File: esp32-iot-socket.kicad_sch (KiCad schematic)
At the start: 2 parts, among them J1 Conn_01x01_Pin, J2 Conn_01x01_Socket

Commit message: viper22as, transformer, hierarchical connections
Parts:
- removed J1: Conn_01x01_Pin, symbol Connector:Conn_01x01_Pin
- removed J2: Conn_01x01_Socket, symbol Connector:Conn_01x01_Socket
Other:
- sheet Microcontroller Section ports: added 3.3V in, Gnd in, TRIAC output, ZV signal in; removed none
- sheet Power Supply Section ports: added 3.3V out, Gnd out, TRIAC in, ZV signal out; removed none
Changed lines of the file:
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@@
 (kicad_sch (version 20230121) (generator eeschema)
   (paper "A4")
-  (symbol (lib_id "Connector:Conn_01x01_Socket") (at 124.46 107.95 0) (unit 1)
-    (in_bom yes) (on_board yes) (dnp no) (fields_autoplaced)
-    (property "Reference" "J2" (at 125.73 106.68 0)
+  (wire (pts (xy 120.65 91.44) (xy 156.21 91.44))
+    (stroke (width 0) (type default))
+  )
+  (wire (pts (xy 120.65 95.25) (xy 156.21 95.25))
+    (stroke (width 0) (type default))
+  )
+  (wire (pts (xy 120.65 105.41) (xy 156.21 105.41))
+    (stroke (width 0) (type default))
+  )
+  (wire (pts (xy 120.65 109.22) (xy 156.21 109.22))
+    (stroke (width 0) (type default))
+  )
+  (sheet (at 156.21 83.82) (size 52.07 39.37) (fields_autoplaced)
+    (stroke (width 0.1524) (type solid))
+    (fill (color 0 0 0 0.0000))
+    (property "Sheetname" "Microcontroller Section" (at 156.21 83.1084 0)
+      (effects (font (size 1.27 1.27)) (justify left bottom))
+    )
+    (property "Sheetfile" "mcu_section.kicad_sch" (at 156.21 123.7746 0)
+      (effects (font (size 1.27 1.27)) (justify left top))
+    )
+    (pin "3.3V in" input (at 156.21 91.44 180)
       (effects (font (size 1.27 1.27)) (justify left))
     )
-    (property "Value" "Conn_01x01_Socket" (at 125.73 109.22 0)
+    (pin "Gnd in" input (at 156.21 95.25 180)
       (effects (font (size 1.27 1.27)) (justify left))
     )
-    (property "Footprint" "" (at 124.46 107.95 0)
-      (effects (font (size 1.27 1.27)) hide)
+    (pin "ZV signal in" input (at 156.21 109.22 180)
+      (effects (font (size 1.27 1.27)) (justify left))
     )
-    (property "Datasheet" "~" (at 124.46 107.95 0)
-      (effects (font (size 1.27 1.27)) hide)
-    )
-    (pin "1")
-    (instances
-      (project "esp32-iot-socket"
-        (path "/45e1e5e5-a388-432c-8d2b-80b7f8345075"
-          (reference "J2") (unit 1)
-        )
-      )
-    )
-  )
-  (symbol (lib_id "Connector:Conn_01x01_Pin") (at 97.79 107.95 0) (unit 1)
-    (in_bom yes) (on_board yes) (dnp no) (fields_autoplaced)
-    (property "Reference" "J1" (at 98.425 102.87 0)
-      (effects (font (size 1.27 1.27)))
-    )
-    (property "Value" "Conn_01x01_Pin" (at 98.425 105.41 0)
-      (effects (font (size 1.27 1.27)))
-    )
-    (property "Footprint" "" (at 97.79 107.95 0)
-      (effects (font (size 1.27 1.27)) hide)
-    )
-    (property "Datasheet" "~" (at 97.79 107.95 0)
-      (effects (font (size 1.27 1.27)) hide)
-    )
-    (pin "1")
-    (instances
-      (project "esp32-iot-socket"
-        (path "/45e1e5e5-a388-432c-8d2b-80b7f8345075"
-          (reference "J1") (unit 1)
-        )
-      )
-    )
-  )
-  (sheet (at 218.44 111.76) (size 52.07 39.37) (fields_autoplaced)
-    (stroke (width 0.1524) (type solid))
-    (fill (color 0 0 0 0.0000))
-    (property "Sheetname" "Microcontroller Section" (at 218.44 111.0484 0)
-      (effects (font (size 1.27 1.27)) (justify left bottom))
-    )
-    (property "Sheetfile" "mcu_section.kicad_sch" (at 218.44 151.7146 0)
-      (effects (font (size 1.27 1.27)) (justify left top))
+    (pin "TRIAC output" output (at 156.21 105.41 180)
+      (effects (font (size 1.27 1.27)) (justify left))
     )
     (instances
@@
     )
   )
-  (sheet (at 218.44 59.69) (size 49.53 34.29) (fields_autoplaced)
+  (sheet (at 71.12 85.09) (size 49.53 34.29) (fields_autoplaced)
     (stroke (width 0.1524) (type solid))
     (fill (color 0 0 0 0.0000))
-    (property "Sheetname" "Power Supply Section" (at 218.44 58.9784 0)
+    (property "Sheetname" "Power Supply Section" (at 71.12 84.3784 0)
       (effects (font (size 1.27 1.27)) (justify left bottom))
     )
-    (property "Sheetfile" "psu.kicad_sch" (at 218.44 94.5646 0)
+    (property "Sheetfile" "psu.kicad_sch" (at 71.12 119.9646 0)
       (effects (font (size 1.27 1.27)) (justify left top))
     )
+    (pin "ZV signal out" output (at 120.65 109.22 0)
+      (effects (font (size 1.27 1.27)) (justify right))
+    )
+    (pin "TRIAC in" input (at 120.65 105.41 0)
+      (effects (font (size 1.27 1.27)) (justify right))
+    )
+    (pin "3.3V out" output (at 120.65 91.44 0)
+      (effects (font (size 1.27 1.27)) (justify right))
+    )
+    (pin "Gnd out" output (at 120.65 95.25 0)
+      (effects (font (size 1.27 1.27)) (justify right))
+    )
     (instances

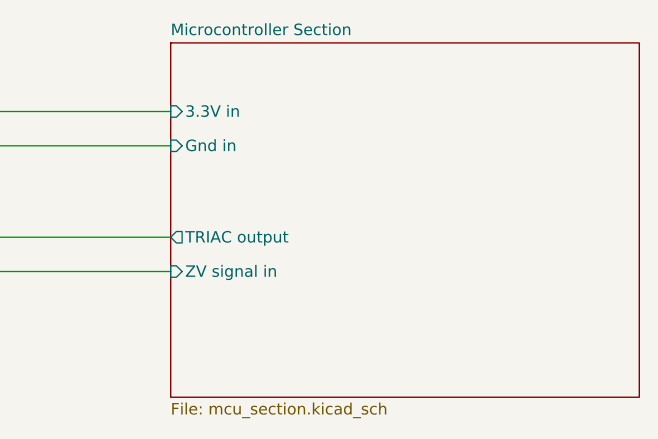
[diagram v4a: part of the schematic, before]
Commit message: completed psu schematic sheet
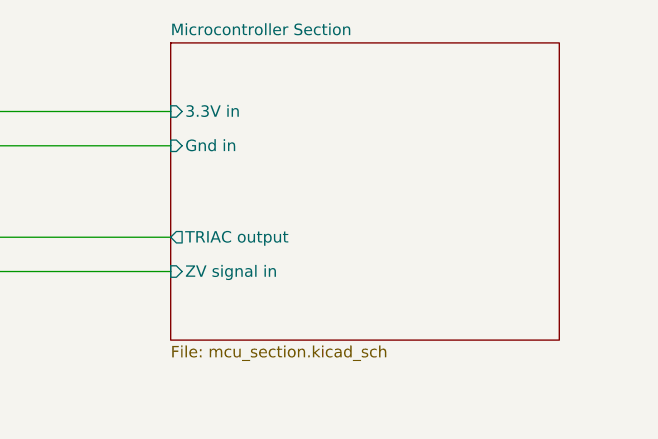
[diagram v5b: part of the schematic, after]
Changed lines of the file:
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@@
     (stroke (width 0) (type default))
   )
-  (sheet (at 156.21 83.82) (size 52.07 39.37) (fields_autoplaced)
+  (sheet (at 156.21 83.82) (size 43.18 33.02) (fields_autoplaced)
     (stroke (width 0.1524) (type solid))
     (fill (color 0 0 0 0.0000))
@@
       (effects (font (size 1.27 1.27)) (justify left bottom))
     )
-    (property "Sheetfile" "mcu_section.kicad_sch" (at 156.21 123.7746 0)
+    (property "Sheetfile" "mcu_section.kicad_sch" (at 156.21 117.4246 0)
       (effects (font (size 1.27 1.27)) (justify left top))
     )

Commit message: schematic completed:
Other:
- sheet Microcontroller Section ports: added ZVC signal in; removed ZV signal in
- sheet Power Supply Section ports: added ZVC signal out; removed ZV signal out
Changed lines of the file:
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@@
 (kicad_sch (version 20230121) (generator eeschema)
   (paper "A4")
-  (wire (pts (xy 120.65 91.44) (xy 156.21 91.44))
+  (wire (pts (xy 116.84 85.09) (xy 180.34 85.09))
     (stroke (width 0) (type default))
   )
-  (wire (pts (xy 120.65 95.25) (xy 156.21 95.25))
+  (wire (pts (xy 116.84 88.9) (xy 180.34 88.9))
     (stroke (width 0) (type default))
   )
-  (wire (pts (xy 120.65 105.41) (xy 156.21 105.41))
+  (wire (pts (xy 116.84 99.06) (xy 180.34 99.06))
     (stroke (width 0) (type default))
   )
-  (wire (pts (xy 120.65 109.22) (xy 156.21 109.22))
+  (wire (pts (xy 116.84 102.87) (xy 180.34 102.87))
     (stroke (width 0) (type default))
   )
-  (sheet (at 156.21 83.82) (size 43.18 33.02) (fields_autoplaced)
+  (sheet (at 180.34 73.66) (size 35.56 41.275) (fields_autoplaced)
     (stroke (width 0.1524) (type solid))
     (fill (color 0 0 0 0.0000))
-    (property "Sheetname" "Microcontroller Section" (at 156.21 83.1084 0)
+    (property "Sheetname" "Microcontroller Section" (at 180.34 72.9484 0)
       (effects (font (size 1.27 1.27)) (justify left bottom))
     )
-    (property "Sheetfile" "mcu_section.kicad_sch" (at 156.21 117.4246 0)
+    (property "Sheetfile" "mcu_section.kicad_sch" (at 180.34 115.5196 0)
       (effects (font (size 1.27 1.27)) (justify left top))
     )
-    (pin "3.3V in" input (at 156.21 91.44 180)
+    (pin "3.3V in" input (at 180.34 85.09 180)
       (effects (font (size 1.27 1.27)) (justify left))
     )
-    (pin "Gnd in" input (at 156.21 95.25 180)
+    (pin "Gnd in" input (at 180.34 88.9 180)
       (effects (font (size 1.27 1.27)) (justify left))
     )
-    (pin "ZV signal in" input (at 156.21 109.22 180)
+    (pin "ZVC signal in" input (at 180.34 102.87 180)
       (effects (font (size 1.27 1.27)) (justify left))
     )
-    (pin "TRIAC output" output (at 156.21 105.41 180)
+    (pin "TRIAC output" output (at 180.34 99.06 180)
       (effects (font (size 1.27 1.27)) (justify left))
     )
@@
     )
   )
-  (sheet (at 71.12 85.09) (size 49.53 34.29) (fields_autoplaced)
+  (sheet (at 71.12 78.74) (size 45.72 31.75) (fields_autoplaced)
     (stroke (width 0.1524) (type solid))
     (fill (color 0 0 0 0.0000))
-    (property "Sheetname" "Power Supply Section" (at 71.12 84.3784 0)
+    (property "Sheetname" "Power Supply Section" (at 71.12 78.0284 0)
       (effects (font (size 1.27 1.27)) (justify left bottom))
     )
-    (property "Sheetfile" "psu.kicad_sch" (at 71.12 119.9646 0)
+    (property "Sheetfile" "psu.kicad_sch" (at 71.12 111.0746 0)
       (effects (font (size 1.27 1.27)) (justify left top))
     )
-    (pin "ZV signal out" output (at 120.65 109.22 0)
+    (pin "TRIAC in" input (at 116.84 99.06 0)
       (effects (font (size 1.27 1.27)) (justify right))
     )
-    (pin "TRIAC in" input (at 120.65 105.41 0)
+    (pin "3.3V out" output (at 116.84 85.09 0)
       (effects (font (size 1.27 1.27)) (justify right))
     )
-    (pin "3.3V out" output (at 120.65 91.44 0)
+    (pin "Gnd out" output (at 116.84 88.9 0)
       (effects (font (size 1.27 1.27)) (justify right))
     )
-    (pin "Gnd out" output (at 120.65 95.25 0)
+    (pin "ZVC signal out" output (at 116.84 102.87 0)
       (effects (font (size 1.27 1.27)) (justify right))
     )
